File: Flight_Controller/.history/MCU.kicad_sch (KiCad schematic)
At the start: 33 parts, among them J10 USB_C_Receptacle_USB2.0_16P, J11 Conn_ARM_SWD_TagConnect_TC203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, J13 SM06B-GHS-TB, J14 VTX, J6 ESC->FC DSHOT and Telem, J7 ELRS Reciever, J9 Camera, SW1 SW_Push, U1 STM32H743VITx, U7 TPD2EUSB30ADRTR

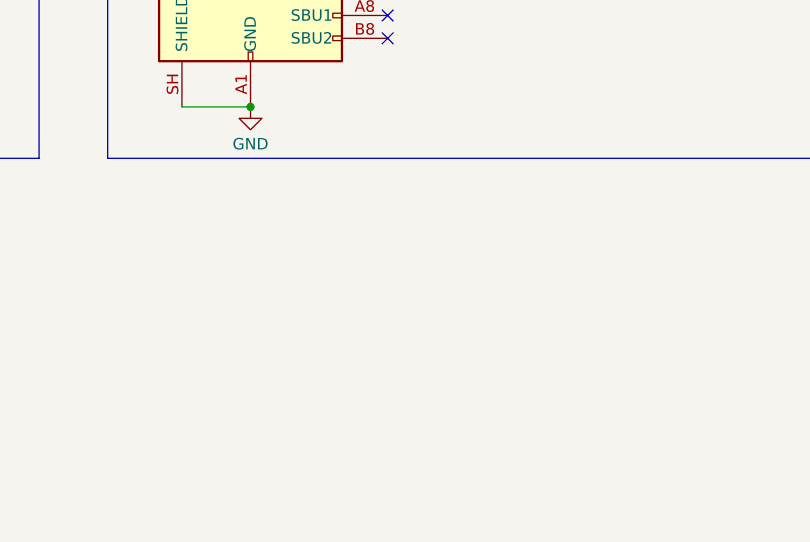
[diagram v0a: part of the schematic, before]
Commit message: Updated buck for 60v spike
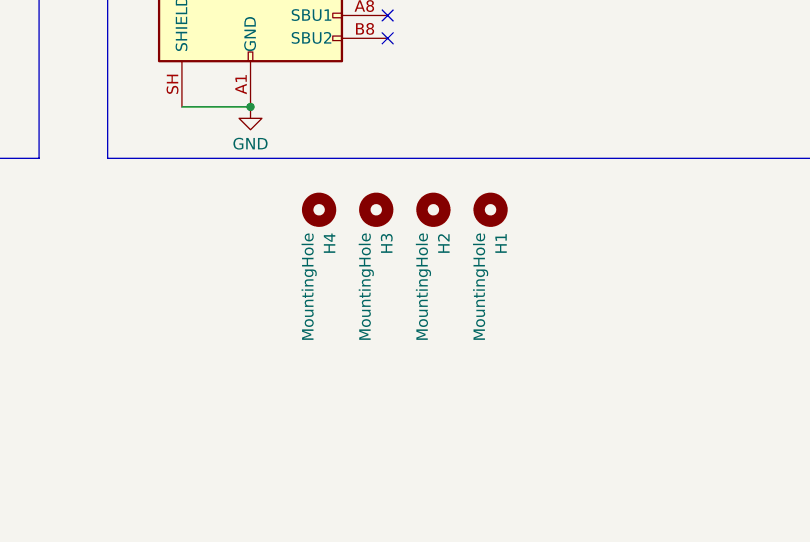
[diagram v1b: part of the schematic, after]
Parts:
- added H1, H2, H3, H4: MountingHole, MountingHole:MountingHole_3.2mm_M3_Pad_Via, symbol Mechanical:MountingHole

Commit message: Initial Layout Done
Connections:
- net MCU_LED: now reaches D1.1, R9.2
- net USB_LED: now reaches D2.1, R10.1
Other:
- moved on the sheet: R10

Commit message: Layout V2
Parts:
- removed D1: Red, PCM_JLCPCB:D_0603, symbol PCM_JLCPCB-Diodes:LED,0603,Red
- removed R9: 150Ω, PCM_JLCPCB:R_0603, symbol PCM_JLCPCB-Resistors:0603,150Ω
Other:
- note removed: "(3.3-2)/0.0075=175"

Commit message: Updated Connector Standard
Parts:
- removed J14: VTX, Connector_JST:JST_GH_SM06B-GHS-TB_1x06-1MP_P1.25mm_Horizontal, symbol Connector_Generic:Conn_01x06
- removed R14: 10kΩ, PCM_JLCPCB:R_0603, symbol PCM_JLCPCB-Resistors:0603,10kΩ
- added D8: Red, PCM_JLCPCB:D_0603, symbol PCM_JLCPCB-Diodes:LED,0603,Red
- added J1: Conn_01x05, symbol Connector_Generic:Conn_01x05
- added R19: 150Ω, PCM_JLCPCB:R_0603, symbol PCM_JLCPCB-Resistors:0603,150Ω
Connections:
- net RST_SW is gone; now on net GND: SW1.1
- net +5V: now also J1.1 (Pin_1)
- net +BATT: now also J6.1 (Pin_1); no longer J6.7 (Pin_7)
- net ADC_CURR: now also J6.3 (Pin_3); no longer J6.1 (Pin_1)
- net ELRS_RX: now also J7.3 (Pin_3); no longer J7.2 (Pin_2)
- net ELRS_TX: now also J7.4 (Pin_4); no longer J7.3 (Pin_3)
- net GND: now also J6.2 (Pin_2), J7.2 (Pin_2), J9.2 (Pin_2), J1.2 (Pin_2), R19.1; no longer J6.8 (Pin_8), J7.4 (Pin_4), J9.3 (Pin_3)
- net M1_DSHOT: now also J6.5 (Pin_5); no longer J6.3 (Pin_3)
- net M2_DSHOT: now also J6.6 (Pin_6); no longer J6.4 (Pin_4)
- net M3_DSHOT: now also J6.7 (Pin_7); no longer J6.5 (Pin_5)
- net M4_DSHOT: now also J6.8 (Pin_8); no longer J6.6 (Pin_6)
- net TELEM_RX: now also J6.4 (Pin_4); no longer J6.2 (Pin_2)
- net VIDEO_IN: now also J9.3 (Pin_3); no longer J9.2 (Pin_2)
- net VIDEO_OUT: now also J1.3 (Pin_3)
- net VTX_RX: now also J1.4 (Pin_4)
- net VTX_TX: now also J1.5 (Pin_5)
- net PB10: now reaches U1.46 (PB10)
- net PB10: now also D8.2
- new net 3V3_LED: D8.1, R19.2
- no-connect marks 52 -> 51
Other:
- note added: "(3.3-2)/0.0075=175"

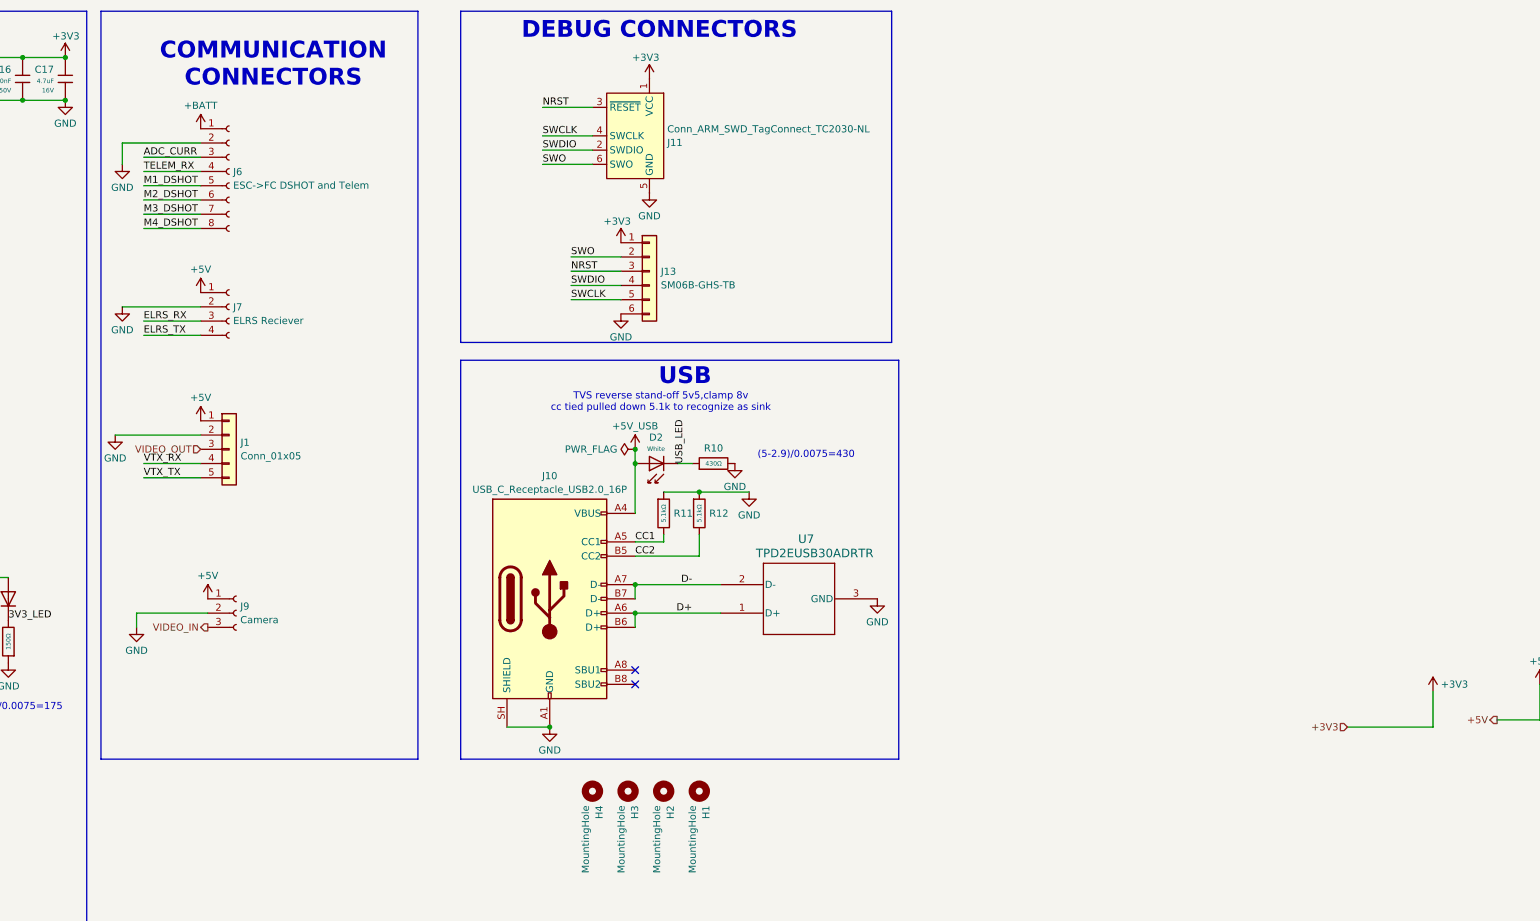
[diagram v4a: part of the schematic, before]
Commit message: Added 9V Buck, GPS + Mag, Digital VTX
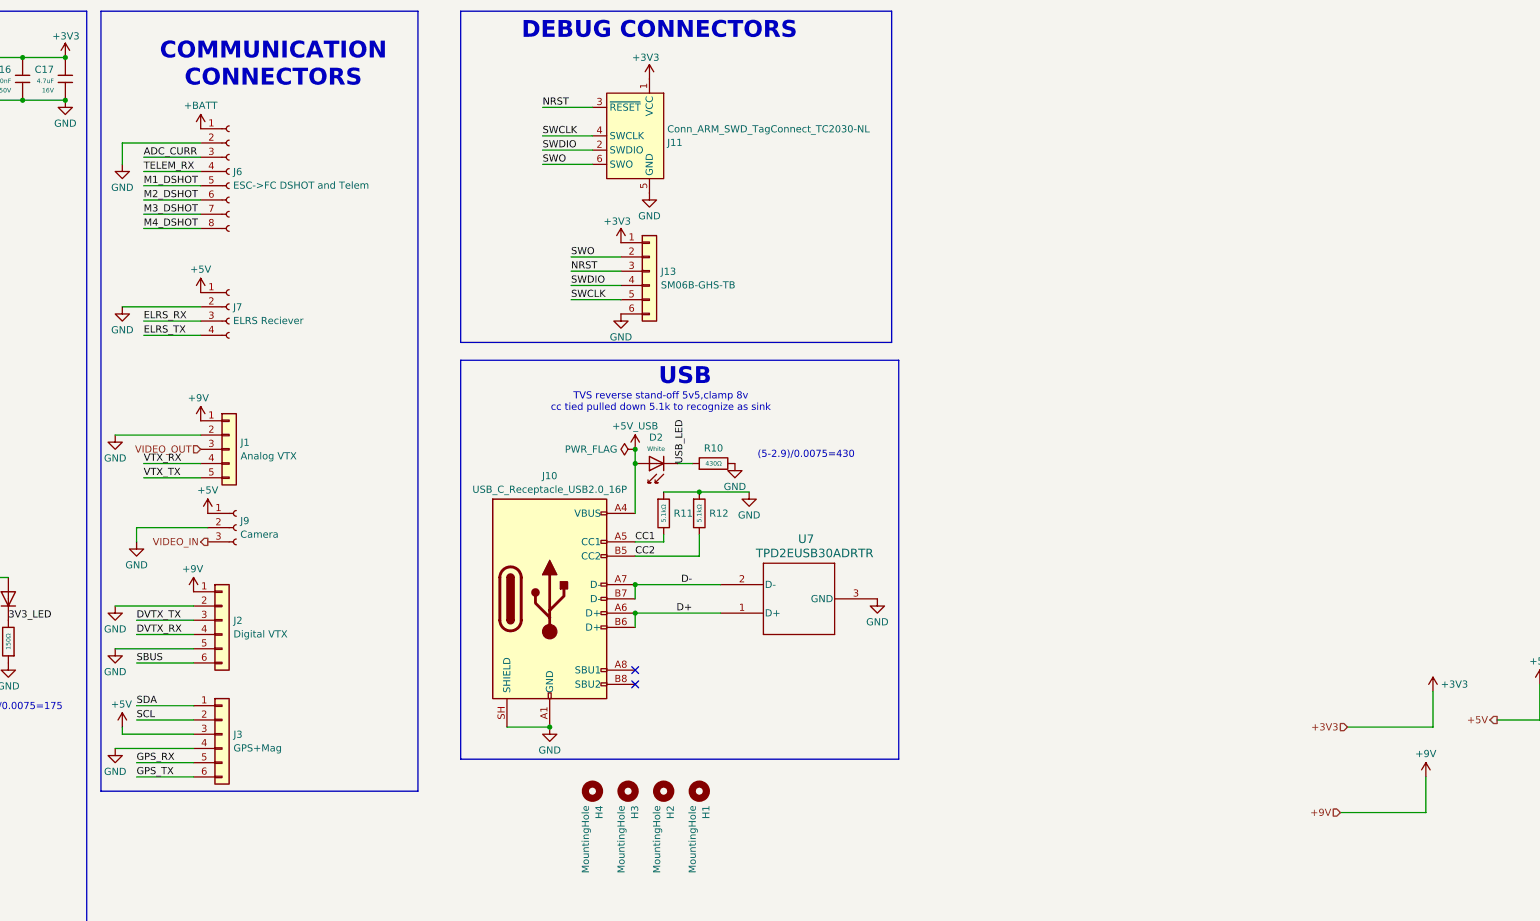
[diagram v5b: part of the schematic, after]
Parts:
- added J2: Digital VTX, symbol Connector_Generic:Conn_01x06
- added J3: GPS+Mag, symbol Connector_Generic:Conn_01x06
- J1: value Conn_01x05 -> Analog VTX
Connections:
- net +5V: now also J3.3 (Pin_3); no longer J1.1 (Pin_1)
- net GND: now also J2.2 (Pin_2), J2.5 (Pin_5), J3.4 (Pin_4)
- new net +9V: J1.1 (Pin_1), J2.1 (Pin_1)
- new net DVTX_RX: J2.4 (Pin_4)
- new net DVTX_TX: J2.3 (Pin_3)
- new net GPS_RX: J3.5 (Pin_5)
- new net GPS_TX: J3.6 (Pin_6)
- new net SBUS: J2.6 (Pin_6)
- new net SCL: J3.2 (Pin_2)
- new net SDA: J3.1 (Pin_1)
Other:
- moved on the sheet: J9

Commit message: Connected all new parts to MCU, added support for hexcopter
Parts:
- removed J6: ESC->FC DSHOT and Telem, Connector_JST:JST_GH_SM08B-GHS-TB_1x08-1MP_P1.25mm_Horizontal, symbol Connector:Conn_01x08_Socket
- added J4: ESC Connector, symbol Connector_Generic:Conn_01x10
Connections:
- net SCL is gone; now on net Mag_SCL: J3.2 (Pin_2)
- net SDA is gone; now on net Mag_SDA: J3.1 (Pin_1)
- net +BATT: now also J4.1 (Pin_1)
- net ADC_CURR: now also J4.3 (Pin_3)
- net DVTX_RX: now also U1.37 (PE7)
- net DVTX_TX: now also U1.38 (PE8)
- net GND: now also J4.2 (Pin_2)
- net GPS_RX: now also U1.92 (PB6)
- net GPS_TX: now also U1.91 (PB5)
- net M1_DSHOT: now also J4.5 (Pin_5)
- net M2_DSHOT: now also J4.6 (Pin_6)
- net M3_DSHOT: now also J4.7 (Pin_7)
- net M4_DSHOT: now also J4.8 (Pin_8)
- net TELEM_RX: now also J4.4 (Pin_4)
- net Mag_SCL: now reaches U1.59 (PD12)
- net Mag_SDA: now reaches U1.60 (PD13)
- net M5_DSHOT: now reaches U1.61 (PD14)
- net M5_DSHOT: now also J4.9 (Pin_9)
- net M6_DSHOT: now reaches U1.62 (PD15)
- net M6_DSHOT: now also J4.10 (Pin_10)
- no-connect marks 51 -> 43
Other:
- note added: "UART_4"
- note added: "UART_5"
- note added: "UART_7"
- note added: "USART_2"
- note added: "USART_3"

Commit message: Updated Footprints
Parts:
- J1: footprint (none) -> Connector_JST:JST_SH_SM05B-SRSS-TB_1x05-1MP_P1.00mm_Horizontal
- J2, J3: footprint (none) -> Connector_JST:JST_SH_SM06B-SRSS-TB_1x06-1MP_P1.00mm_Horizontal
- J4: footprint (none) -> Connector_JST:JST_SH_SM10B-SRSS-TB_1x10-1MP_P1.00mm_Horizontal
- J7: footprint Connector_JST:JST_GH_SM04B-GHS-TB_1x04-1MP_P1.25mm_Horizontal -> Connector_JST:JST_SH_SM04B-SRSS-TB_1x04-1MP_P1.00mm_Horizontal
- J9: footprint Connector_JST:JST_GH_SM03B-GHS-TB_1x03-1MP_P1.25mm_Horizontal -> Connector_JST:JST_SH_SM03B-SRSS-TB_1x03-1MP_P1.00mm_Horizontal
- SW1: footprint Resistor_SMD:R_0805_2012Metric -> Flight_Controller:SW_TS-1088-AR02016
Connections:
- net SBUS: now also U1.64 (PC7)
- no-connect marks 43 -> 42
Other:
- note added: "USART_6"
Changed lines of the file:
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@@
 		)
 	)
+	(text "USART_6"
+		(exclude_from_sim no)
+		(at 111.76 154.432 0)
+		(effects
+			(font
+				(size 1.27 1.27)
+			)
+		)
+	)
 	(text "DEBUG CONNECTORS"
 		(exclude_from_sim no)
@@
 	)
 	(no_connect
-		(at 97.79 154.94)
-	)
-	(no_connect
 		(at 97.79 71.12)
 	)
@@
 	(wire
 		(pts
+			(xy 97.79 154.94) (xy 105.41 154.94)
+		)
+		(stroke
+			(width 0)
+			(type default)
+		)
+	)
+	(wire
+		(pts
 			(xy 107.95 109.22) (xy 97.79 109.22)
 		)
@@
 		)
 	)
+	(label "SBUS"
+		(at 105.41 154.94 180)
+		(effects
+			(font
+				(size 1.27 1.27)
+			)
+			(justify right bottom)
+		)
+	)
 	(label "VTX_RX"
 		(at 111.76 53.34 180)
@@
 			)
 		)
-		(property "Footprint" "Resistor_SMD:R_0805_2012Metric"
+		(property "Footprint" "Flight_Controller:SW_TS-1088-AR02016"
 			(at 36.83 38.1 0)
 			(hide yes)
@@
 			)
 		)
-		(property "Footprint" ""
+		(property "Footprint" "Connector_JST:JST_SH_SM05B-SRSS-TB_1x05-1MP_P1.00mm_Horizontal"
 			(at 160.02 96.52 0)
 			(hide yes)
@@
 			)
 		)
-		(property "Footprint" "Connector_JST:JST_GH_SM04B-GHS-TB_1x04-1MP_P1.25mm_Horizontal"
+		(property "Footprint" "Connector_JST:JST_SH_SM04B-SRSS-TB_1x04-1MP_P1.00mm_Horizontal"
 			(at 160.02 71.12 0)
 			(hide yes)
@@
 			)
 		)
-		(property "Footprint" ""
+		(property "Footprint" "Connector_JST:JST_SH_SM06B-SRSS-TB_1x06-1MP_P1.00mm_Horizontal"
 			(at 158.75 147.32 0)
 			(hide yes)
@@
 			)
 		)
-		(property "Footprint" ""
+		(property "Footprint" "Connector_JST:JST_SH_SM10B-SRSS-TB_1x10-1MP_P1.00mm_Horizontal"
 			(at 160.02 49.53 0)
 			(hide yes)
@@
 			)
 		)
-		(property "Footprint" "Connector_JST:JST_GH_SM03B-GHS-TB_1x03-1MP_P1.25mm_Horizontal"
+		(property "Footprint" "Connector_JST:JST_SH_SM03B-SRSS-TB_1x03-1MP_P1.00mm_Horizontal"
 			(at 161.29 110.49 0)
 			(hide yes)
@@
 			)
 		)
-		(property "Footprint" ""
+		(property "Footprint" "Connector_JST:JST_SH_SM06B-SRSS-TB_1x06-1MP_P1.00mm_Horizontal"
 			(at 158.75 127 0)
 			(hide yes)

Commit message: Updated Layout to 60x30
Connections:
- net 3V3_LED renamed MCU_LED
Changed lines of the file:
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@@
 		)
 	)
-	(label "3V3_LED"
+	(label "MCU_LED"
 		(at 120.65 127 0)
 		(effects
